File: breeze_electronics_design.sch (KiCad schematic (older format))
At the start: 100 parts, among them U1 STM32F103T8U6TR

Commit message: Modify the schematic of wireless
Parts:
- removed C? (x2): 0.1UF, symbol Capacitance
- added C?: 0.1UF, C0402, symbol Capacitance
- added C?: 2.2UF, C0402, symbol Capacitance
- A?: footprint (none) -> AN950-245
- C? (x7): footprint (none) -> C0402
- L? (x3): footprint (none) -> L0402
- R?: footprint (none) -> R0402
- U?: footprint (none) -> BT_UART_13D5X18D5MM
- X?: value XTAL -> 16MHZ; footprint (none) -> XTAL_32X25
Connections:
- net VCC3.3 is gone; now on net +3V3: U?.18 (VDD3)
- net +3V3: now also C?.1, C?.1
- net GND: now also C?.2, C?.2
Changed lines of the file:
@@
 	1    0    0    -1
 $EndComp
-Text Label 8650 2200 2    60   ~ 0
+Text Label 8650 2200 0    60   ~ 0
 CE
-Text Label 8700 2300 2    60   ~ 0
-CSN
-Text Label 8700 2400 2    60   ~ 0
-SCK
-Text Label 8750 2500 2    60   ~ 0
+Text Label 8650 2500 0    60   ~ 0
 MOSI
-Text Label 8750 2600 2    60   ~ 0
+Text Label 8650 2600 0    60   ~ 0
 MISO
 $Comp
@@
 U 1 1 57B3AC90
 P 9450 1350
-F 0 "C?" H 9200 1450 50  0000 L CNN
+F 0 "C?" H 9175 1425 50  0000 L CNN
 F 1 "2.2UF" H 9100 1350 50  0000 L CNN
-F 2 "" H 9450 1350 50  0000 C CNN
+F 2 "C0402" H 9200 1275 50  0000 C CNN
 F 3 "" H 9450 1350 50  0000 C CNN
 	1    9450 1350
@@
 F 0 "R?" H 9780 1370 50  0000 L CNN
 F 1 "22K" H 9780 1310 50  0000 L CNN
-F 2 "" H 9750 1350 50  0000 C CNN
+F 2 "R0402" H 9900 1250 50  0000 C CNN
 F 3 "" H 9750 1350 50  0000 C CNN
 	1    9750 1350
@@
 	-1   0    0    1
 $EndComp
-Text Label 9550 1050 0    60   ~ 0
-VCC3.3
 Text Label 9350 3500 1    60   ~ 0
 NRF_IRQ
@@
 U 1 1 57B437FC
 P 10350 3950
-F 0 "X?" H 10100 4150 60  0000 C CNN
-F 1 "XTAL" H 10350 3750 60  0000 C CNN
-F 2 "" H 10350 4000 60  0000 C CNN
+F 0 "X?" H 10100 4100 60  0000 C CNN
+F 1 "16MHZ" H 10350 3800 60  0000 C CNN
+F 2 "XTAL_32X25" H 10350 3725 60  0000 C CNN
 F 3 "" H 10350 4000 60  0000 C CNN
 	1    10350 3950
@@
 F 0 "C?" V 9450 3875 50  0000 L CNN
 F 1 "22PF" V 9375 3775 50  0000 L CNN
-F 2 "" H 9500 4000 50  0000 C CNN
+F 2 "C0402" V 9300 3850 50  0000 C CNN
 F 3 "" H 9500 4000 50  0000 C CNN
 	1    9500 4000
@@
 F 0 "C?" V 11100 3775 50  0000 L CNN
 F 1 "22PF" V 11025 3675 50  0000 L CNN
-F 2 "" H 11150 3900 50  0000 C CNN
+F 2 "C0402" V 10950 3750 50  0000 C CNN
 F 3 "" H 11150 3900 50  0000 C CNN
 	1    11150 3900
@@
 F 0 "C?" H 10660 2920 50  0000 L CNN
 F 1 "2.2NF" H 10660 2770 50  0000 L CNN
-F 2 "" H 10650 2850 50  0000 C CNN
+F 2 "C0402" H 10775 2700 50  0000 C CNN
 F 3 "" H 10650 2850 50  0000 C CNN
 	1    10650 2850
@@
 F 0 "C?" H 10910 2920 50  0000 L CNN
 F 1 "4.7PF" H 10910 2770 50  0000 L CNN
-F 2 "" H 10900 2850 50  0000 C CNN
+F 2 "C0402" H 11025 2700 50  0000 C CNN
 F 3 "" H 10900 2850 50  0000 C CNN
 	1    10900 2850
@@
 P 10900 2200
 F 0 "L?" V 10950 2125 50  0000 C CNN
-F 1 "2.7NH" V 10850 2050 50  0000 C CNN
-F 2 "" H 10900 2200 50  0000 C CNN
+F 1 "2.7NH" V 10875 2050 50  0000 C CNN
+F 2 "L0402" V 10800 2050 50  0000 C CNN
 F 3 "" H 10900 2200 50  0000 C CNN
 	1    10900 2200
@@
 P 10900 1400
 F 0 "L?" V 10950 1325 50  0000 C CNN
-F 1 "8.2NH" V 10850 1250 50  0000 C CNN
-F 2 "" H 10900 1400 50  0000 C CNN
+F 1 "8.2NH" V 10875 1250 50  0000 C CNN
+F 2 "L0402" V 10800 1250 50  0000 C CNN
 F 3 "" H 10900 1400 50  0000 C CNN
 	1    10900 1400
@@
 U 1 1 57B4BB4C
 P 11350 1050
-F 0 "L?" H 11175 1250 50  0000 C CNN
-F 1 "3.9NH" H 11250 1150 50  0000 C CNN
-F 2 "" H 11350 1050 50  0000 C CNN
+F 0 "L?" H 11350 1250 50  0000 C CNN
+F 1 "3.9NH" H 11350 1150 50  0000 C CNN
+F 2 "L0402" H 11350 1000 50  0000 C CNN
 F 3 "" H 11350 1050 50  0000 C CNN
 	1    11350 1050
@@
 U 1 1 57B4C7A5
 P 11800 1050
-F 0 "C?" V 12000 1175 50  0000 L CNN
-F 1 "1.5PF" V 11900 1050 50  0000 L CNN
-F 2 "" H 11800 1050 50  0000 C CNN
+F 0 "C?" V 12000 1000 50  0000 L CNN
+F 1 "1.5PF" V 11900 950 50  0000 L CNN
+F 2 "C0402" V 11700 1050 50  0000 C CNN
 F 3 "" H 11800 1050 50  0000 C CNN
 	1    11800 1050
@@
 F 0 "C?" H 12010 1320 50  0000 L CNN
 F 1 "1PF" H 12010 1170 50  0000 L CNN
-F 2 "" H 12000 1250 50  0000 C CNN
+F 2 "C0402" H 12125 1100 50  0000 C CNN
 F 3 "" H 12000 1250 50  0000 C CNN
 	1    12000 1250
@@
 F 0 "A?" H 12450 1250 60  0000 C CNN
 F 1 "Antenna" H 12650 850 60  0000 C CNN
-F 2 "" H 11750 950 60  0000 C CNN
+F 2 "AN950-245" H 12650 750 60  0000 C CNN
 F 3 "" H 11750 950 60  0000 C CNN
 	1    12650 1050
-	1    0    0    -1
-$EndComp
-$Comp
-L Capacitance C?
-U 1 1 57B4EC68
-P 12450 1950
-F 0 "C?" H 12460 2020 50  0000 L CNN
-F 1 "0.1UF" H 12460 1870 50  0000 L CNN
-F 2 "" H 12450 1950 50  0000 C CNN
-F 3 "" H 12450 1950 50  0000 C CNN
-	1    12450 1950
-	1    0    0    -1
-$EndComp
-$Comp
-L Capacitance C?
-U 1 1 57B4EE47
-P 12750 1950
-F 0 "C?" H 12760 2020 50  0000 L CNN
-F 1 "0.1UF" H 12760 1870 50  0000 L CNN
-F 2 "" H 12750 1950 50  0000 C CNN
-F 3 "" H 12750 1950 50  0000 C CNN
-	1    12750 1950
-	1    0    0    -1
-$EndComp
-$Comp
-L GND #PWR?
-U 1 1 57B4F087
-P 12600 2150
-F 0 "#PWR?" H 12600 1900 50  0001 C CNN
-F 1 "GND" H 12600 2000 50  0000 C CNN
-F 2 "" H 12600 2150 50  0000 C CNN
-F 3 "" H 12600 2150 50  0000 C CNN
-	1    12600 2150
-	1    0    0    -1
-$EndComp
-$Comp
-L +3.3V #PWR?
-U 1 1 57B4F0F9
-P 12600 1750
-F 0 "#PWR?" H 12600 1600 50  0001 C CNN
-F 1 "+3.3V" H 12600 1890 50  0000 C CNN
-F 2 "" H 12600 1750 50  0000 C CNN
-F 3 "" H 12600 1750 50  0000 C CNN
-	1    12600 1750
 	1    0    0    -1
 $EndComp
@@
 U 1 1 57B51355
 P 12600 3000
-F 0 "U?" H 12250 3450 60  0000 C CNN
-F 1 "HM-06-BT" H 12600 2450 60  0000 C CNN
-F 2 "" H 12600 3050 60  0000 C CNN
+F 0 "U?" H 12250 3400 60  0000 C CNN
+F 1 "HM-06-BT" H 12600 2500 60  0000 C CNN
+F 2 "BT_UART_13D5X18D5MM" H 12600 2400 60  0000 C CNN
 F 3 "" H 12600 3050 60  0000 C CNN
 	1    12600 3000
@@
 	6300 2400 6300 2700
 Wire Wire Line
-	8550 2600 8850 2600
-Wire Wire Line
-	8550 2500 8850 2500
-Wire Wire Line
-	8550 2400 8850 2400
-Wire Wire Line
-	8550 2300 8850 2300
-Wire Wire Line
-	8550 2200 8850 2200
-Wire Wire Line
 	9450 1450 9450 1750
 Wire Wire Line
@@
 	12000 1350 12000 1450
 Connection ~ 12000 1050
-Wire Wire Line
-	12450 1850 12450 1750
-Wire Wire Line
-	12450 1750 12750 1750
-Wire Wire Line
-	12750 1750 12750 1850
-Connection ~ 12600 1750
-Wire Wire Line
-	12450 2050 12450 2150
-Wire Wire Line
-	12450 2150 12750 2150
-Wire Wire Line
-	12750 2150 12750 2050
-Connection ~ 12600 2150
 Wire Wire Line
 	600  1050 600  1150
@@
 Text Label 2050 4675 0    60   ~ 0
 VBUS
+Wire Wire Line
+	8650 2500 8850 2500
+Wire Wire Line
+	8650 2600 8850 2600
+Text Label 8650 2400 0    60   ~ 0
+SCK
+Wire Wire Line
+	8650 2400 8850 2400
+Text Label 8650 2300 0    60   ~ 0
+CSN
+Wire Wire Line
+	8650 2300 8850 2300
+Wire Wire Line
+	8650 2200 8850 2200
+$Comp
+L +3.3V #PWR?
+U 1 1 57BA0919
+P 9550 1050
+F 0 "#PWR?" H 9550 900 50  0001 C CNN
+F 1 "+3.3V" H 9550 1190 50  0000 C CNN
+F 2 "" H 9550 1050 50  0000 C CNN
+F 3 "" H 9550 1050 50  0000 C CNN
+	1    9550 1050
+	1    0    0    -1
+$EndComp
+$Comp
+L Capacitance C?
+U 1 1 57BAF0AE
+P 12150 2000
+F 0 "C?" H 12160 2070 50  0000 L CNN
+F 1 "0.1UF" H 12150 1925 50  0000 L CNN
+F 2 "C0402" H 12275 1850 50  0000 C CNN
+F 3 "" H 12150 2000 50  0000 C CNN
+	1    12150 2000
+	1    0    0    -1
+$EndComp
+$Comp
+L Capacitance C?
+U 1 1 57BAF0B5
+P 12550 2000
+F 0 "C?" H 12560 2070 50  0000 L CNN
+F 1 "2.2UF" H 12550 1925 50  0000 L CNN
+F 2 "C0402" H 12675 1850 50  0000 C CNN
+F 3 "" H 12550 2000 50  0000 C CNN
+	1    12550 2000
+	1    0    0    -1
+$EndComp
+$Comp
+L GND #PWR?
+U 1 1 57BAF0BC
+P 12350 2300
+F 0 "#PWR?" H 12350 2050 50  0001 C CNN
+F 1 "GND" H 12350 2150 50  0000 C CNN
+F 2 "" H 12350 2300 50  0000 C CNN
+F 3 "" H 12350 2300 50  0000 C CNN
+	1    12350 2300
+	1    0    0    -1
+$EndComp
+$Comp
+L +3.3V #PWR?
+U 1 1 57BAF0C2
+P 12350 1750
+F 0 "#PWR?" H 12350 1600 50  0001 C CNN
+F 1 "+3.3V" H 12350 1890 50  0000 C CNN
+F 2 "" H 12350 1750 50  0000 C CNN
+F 3 "" H 12350 1750 50  0000 C CNN
+	1    12350 1750
+	1    0    0    -1
+$EndComp
+Wire Wire Line
+	12150 2100 12150 2200
+Wire Wire Line
+	12150 1900 12150 1850
+Wire Wire Line
+	12550 1850 12550 1900
+Wire Wire Line
+	12550 2200 12550 2100
+Wire Wire Line
+	12150 2200 12550 2200
+Wire Wire Line
+	12350 2200 12350 2300
+Connection ~ 12350 2200
+Wire Wire Line
+	12150 1850 12550 1850
+Wire Wire Line
+	12350 1750 12350 1850
+Connection ~ 12350 1850
 $EndSCHEMATC

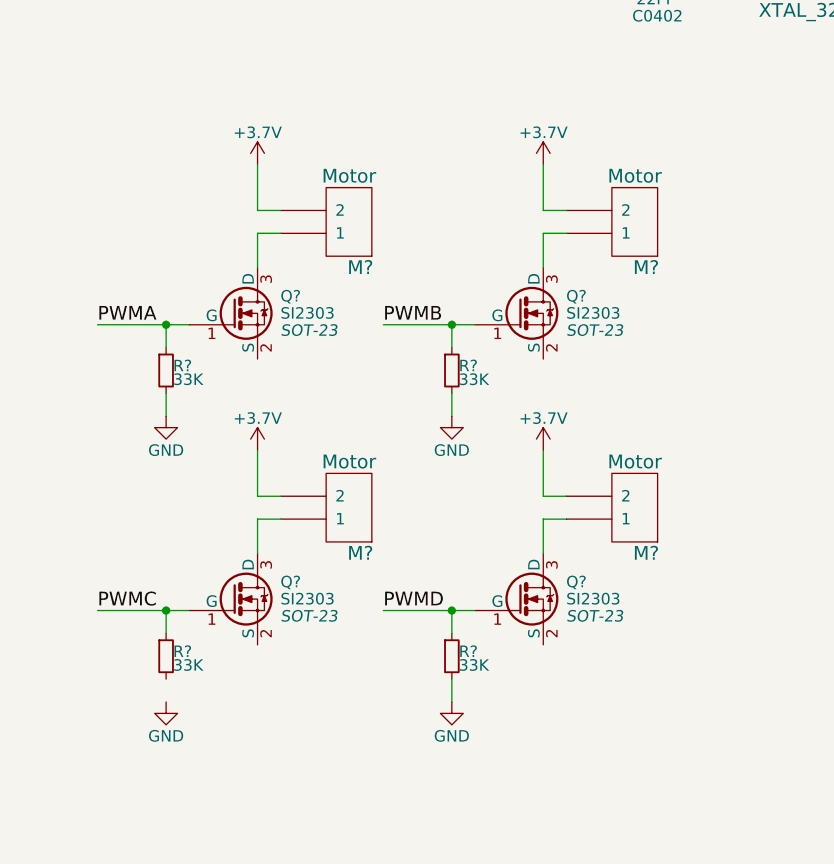
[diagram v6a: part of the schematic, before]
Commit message: Modify the schematic of motor
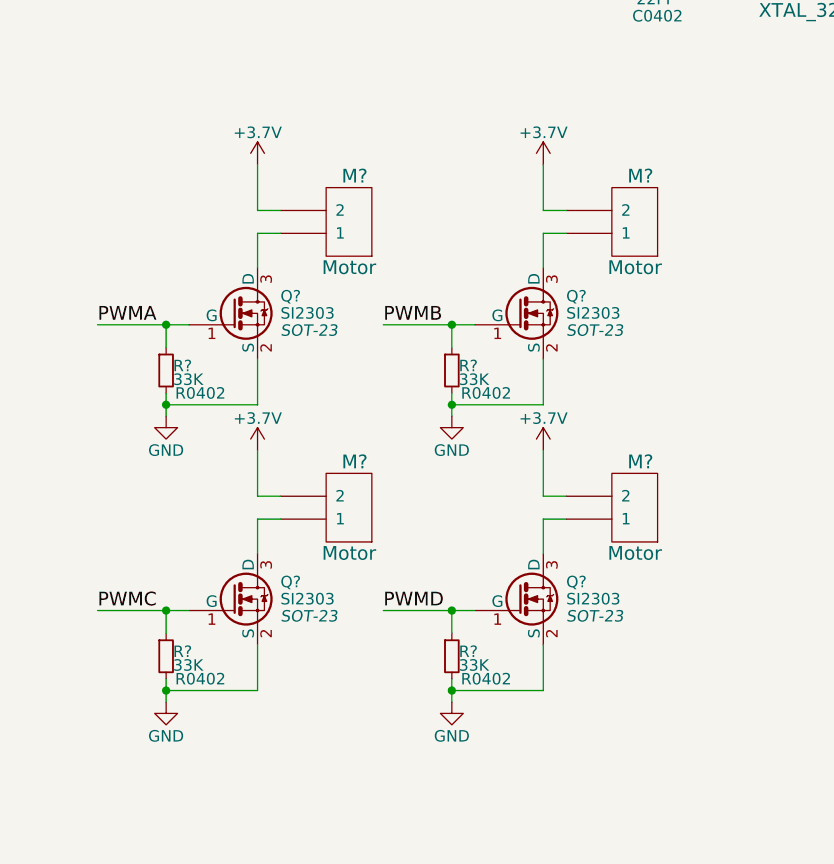
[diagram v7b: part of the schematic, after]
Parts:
- R? (x4): footprint (none) -> R0402
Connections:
- net GND: now also Q?.2 (S), Q?.2 (S), Q?.2 (S), Q?.2 (S), R?.2
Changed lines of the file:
@@
 U 1 1 57B540B6
 P 8300 5100
-F 0 "M?" H 8250 5300 60  0000 C CNN
-F 1 "Motor" H 8300 4900 60  0000 C CNN
+F 0 "M?" H 8275 4900 60  0000 C CNN
+F 1 "Motor" H 8300 5300 60  0000 C CNN
 F 2 "" H 8300 5100 60  0000 C CNN
 F 3 "" H 8300 5100 60  0000 C CNN
@@
 F 0 "R?" H 7530 5770 50  0000 L CNN
 F 1 "33K" H 7530 5710 50  0000 L CNN
-F 2 "" H 7500 5750 50  0000 C CNN
+F 2 "R0402" H 7650 5650 50  0000 C CNN
 F 3 "" H 7500 5750 50  0000 C CNN
 	1    7500 5750
@@
 U 1 1 57B5A56D
 P 9550 5100
-F 0 "M?" H 9500 5300 60  0000 C CNN
-F 1 "Motor" H 9550 4900 60  0000 C CNN
+F 0 "M?" H 9525 4900 60  0000 C CNN
+F 1 "Motor" H 9550 5300 60  0000 C CNN
 F 2 "" H 9550 5100 60  0000 C CNN
 F 3 "" H 9550 5100 60  0000 C CNN
@@
 F 0 "R?" H 8780 5770 50  0000 L CNN
 F 1 "33K" H 8780 5710 50  0000 L CNN
-F 2 "" H 8750 5750 50  0000 C CNN
+F 2 "R0402" H 8900 5650 50  0000 C CNN
 F 3 "" H 8750 5750 50  0000 C CNN
 	1    8750 5750
@@
 U 1 1 57B5AFF6
 P 8300 6350
-F 0 "M?" H 8250 6550 60  0000 C CNN
-F 1 "Motor" H 8300 6150 60  0000 C CNN
+F 0 "M?" H 8275 6150 60  0000 C CNN
+F 1 "Motor" H 8300 6550 60  0000 C CNN
 F 2 "" H 8300 6350 60  0000 C CNN
 F 3 "" H 8300 6350 60  0000 C CNN
@@
 F 0 "R?" H 7530 7020 50  0000 L CNN
 F 1 "33K" H 7530 6960 50  0000 L CNN
-F 2 "" H 7500 7000 50  0000 C CNN
+F 2 "R0402" H 7650 6900 50  0000 C CNN
 F 3 "" H 7500 7000 50  0000 C CNN
 	1    7500 7000
@@
 U 1 1 57B5B269
 P 9550 6350
-F 0 "M?" H 9500 6550 60  0000 C CNN
-F 1 "Motor" H 9550 6150 60  0000 C CNN
+F 0 "M?" H 9525 6150 60  0000 C CNN
+F 1 "Motor" H 9550 6550 60  0000 C CNN
 F 2 "" H 9550 6350 60  0000 C CNN
 F 3 "" H 9550 6350 60  0000 C CNN
@@
 F 0 "R?" H 8780 7020 50  0000 L CNN
 F 1 "33K" H 8780 6960 50  0000 L CNN
-F 2 "" H 8750 7000 50  0000 C CNN
+F 2 "R0402" H 8900 6900 50  0000 C CNN
 F 3 "" H 8750 7000 50  0000 C CNN
 	1    8750 7000
@@
 	12350 1750 12350 1850
 Connection ~ 12350 1850
+Wire Wire Line
+	7500 7100 7500 7200
+Wire Wire Line
+	7500 5900 7900 5900
+Wire Wire Line
+	7900 5900 7900 5700
+Connection ~ 7500 5900
+Wire Wire Line
+	8750 5900 9150 5900
+Wire Wire Line
+	9150 5900 9150 5700
+Connection ~ 8750 5900
+Wire Wire Line
+	7500 7150 7900 7150
+Wire Wire Line
+	7900 7150 7900 6950
+Connection ~ 7500 7150
+Wire Wire Line
+	8750 7150 9150 7150
+Wire Wire Line
+	9150 7150 9150 6950
+Connection ~ 8750 7150
 $EndSCHEMATC
